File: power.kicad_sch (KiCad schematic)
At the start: 24 parts

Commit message: regulators
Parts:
- removed C_BECFC1, C_BECVTX1: 4u7, Capacitor_SMD:C_1206_3216Metric, symbol Device:C_Small
- removed C_BECFC2, C_BECVTX2: 100n, Capacitor_SMD:C_1206_3216Metric, symbol Device:C_Small
- removed C_BECFC3, C_BECVTX3: 1u, Capacitor_SMD:C_1206_3216Metric, symbol Device:C_Small
- removed C_BECFC4, C_BECFC5: 33u, Capacitor_SMD:C_1206_3216Metric, symbol Device:C_Small
- removed C_BECVTX4, C_BECVTX5, C_BECVTX6: 10u, Capacitor_SMD:C_1206_3216Metric, symbol Device:C_Small
- removed R_BECFC1: 41k2, Resistor_SMD:R_0402_1005Metric, symbol Device:R_Small
- removed R_BECFC2, R_BECVTX3: 10k, Resistor_SMD:R_0402_1005Metric, symbol Device:R_Small
- removed R_BECFC3: 12k1, Resistor_SMD:R_0402_1005Metric, symbol Device:R_Small
- removed R_BECVTX1: 10k5, Resistor_SMD:R_0402_1005Metric, symbol Device:R_Small
- removed R_BECVTX2: 80k6, Resistor_SMD:R_0402_1005Metric, symbol Device:R_Small
- removed U_BEC_FC_5V_1, U_BEC_VTX_9V_1: TPSM33625RDNR, RDN0011A-MFG, symbol custom_Library:TPSM33625RDNR
- added 5_C1, 5_C7: 10u, Capacitor_SMD:C_0603_1608Metric, symbol Device:C
- added 5_C10, 5_C11, 5_C4, 5_C5: 22u, Capacitor_SMD:C_0805_2012Metric, symbol Device:C
- added 5_C12, 5_C6: 75p, Capacitor_SMD:C_0402_1005Metric, symbol Device:C
- added 5_C2, 5_C3, 5_C8, 5_C9: 0.1u, Capacitor_SMD:C_0402_1005Metric, symbol Device:C
- added 5_R1, 5_R5: 511k, Resistor_SMD:R_0603_1608Metric, symbol Device:R
- added 5_R2, 5_R6: 105k, Resistor_SMD:R_0603_1608Metric, symbol Device:R
- added 5_R3, 5_R7: 100k, Resistor_SMD:R_0603_1608Metric, symbol Device:R
- added 5_R4: 13.3k, Resistor_SMD:R_0402_1005Metric, symbol Device:R
- added 5_R8: 7k, Resistor_SMD:R_0402_1005Metric, symbol Device:R
- added L1, L2: 10, Capacitor_SMD:C_0603_1608Metric, symbol Device:L
- added U4, U5: TPS54302DDCR, Package_TO_SOT_SMD:SOT-23-6, symbol Regulator_Switching:TPS54302
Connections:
- net 5V_BEC: now also 5_C10.1, 5_C11.1, 5_C12.1, 5_C4.1, 5_C5.1, 5_C6.1, 5_R3.1, 5_R7.1, L1.2, L2.2
- net GND: now also 5_C1.2, 5_C10.2, 5_C11.2, 5_C2.2, 5_C4.2, 5_C5.2, 5_C7.2, 5_C8.2, 5_R2.2, 5_R4.2, 5_R6.2, 5_R8.2, U4.1 (GND), U5.1 (GND)
- net Vin_LIPO: now also 5_C1.1, 5_C2.1, 5_C7.1, 5_C8.1, 5_R1.1, 5_R5.1, U4.3 (VIN), U5.3 (VIN)
- new net: 5_C3.2, L1.1, U4.2 (SW)
- new net: 5_C6.2, 5_R3.2, 5_R4.1, U4.4 (FB)
- new net: 5_R1.2, 5_R2.1, U4.5 (EN)
- new net: 5_C3.1, U4.6 (BOOT)
- new net: 5_C9.2, L2.1, U5.2 (SW)
- new net: 5_C12.2, 5_R7.2, 5_R8.1, U5.4 (FB)
- new net: 5_R5.2, 5_R6.1, U5.5 (EN)
- new net: 5_C9.1, U5.6 (BOOT)
- no-connect marks 5 -> 1
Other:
- note added: "BAT -> 5V"
- note added: "BAT -> 9V"
- note removed: "FC: BAT->5.1V@2.5A: TPSM33625RDNR"
- note removed: "VTX: BAT->9V@2.5A (DJI:~1A@9V) TPSM33625RDNR"

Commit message: boom boom
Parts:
- L1: value 10 -> 10u
- L2: value 10 -> 15u
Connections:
- net 5V_BEC: no longer 5_C10.1, 5_C11.1, 5_C12.1, 5_R7.1, L2.2
- new net 9V_BEC: 5_C10.1, 5_C11.1, 5_C12.1, 5_R7.1, L2.2
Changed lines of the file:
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@@
 		)
 	)
-	(global_label "5V_BEC"
+	(global_label "9V_BEC"
 		(shape input)
 		(at 260.35 119.38 0)
@@
 			)
 		)
-		(property "Value" "10"
+		(property "Value" "10u"
 			(at 226.06 41.91 90)
 			(effects
@@
 			)
 		)
-		(property "Value" "10"
+		(property "Value" "15u"
 			(at 226.06 116.84 90)
 			(effects

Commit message: labels
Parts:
- 5V_C2: renamed from 5_C2; value 0.1u -> 0u1
- 5V_C3: renamed from 5_C3; value 0.1u -> 0u1
- 9V_C2: renamed from 5_C8; value 0.1u -> 0u1
- 9V_C3: renamed from 5_C9; value 0.1u -> 0u1
- renumbered C2_LDO1 to 3V3_C2, C1_LDO1 to 3v3_C1, 5_C1 to 5V_C1, 5_C4 to 5V_C4, 5_C5 to 5V_C5, 5_C6 to 5V_C6, L1 to 5V_L1, 5_R1 to 5V_R1, 5_R2 to 5V_R2, 5_R3 to 5V_R3, 5_R4 to 5V_R4, 5_C7 to 9V_C1, 5_C10 to 9V_C4, 5_C11 to 9V_C5, 5_C12 to 9V_C6, L2 to 9V_L1, 5_R5 to 9V_R1, 5_R6 to 9V_R2, 5_R7 to 9V_R3, 5_R8 to 9V_R4, U_LDO1 to U_3V3
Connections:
- net 3V3_MCU_OSD renamed 3.3V
- net Vin_LIPO renamed LIPO
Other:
- note added: "5V -> 3V3 @500mA"
- note removed: "FC LDO: 5V bus -> 3V3 @500mA"

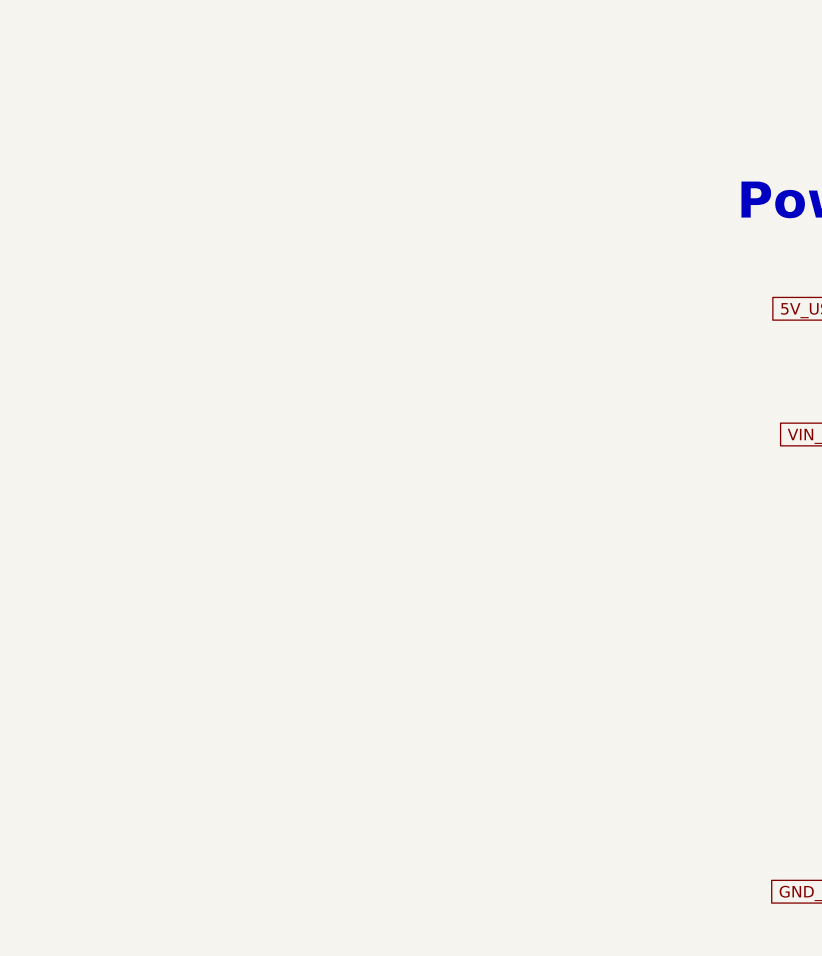
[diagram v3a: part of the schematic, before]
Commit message: power mux
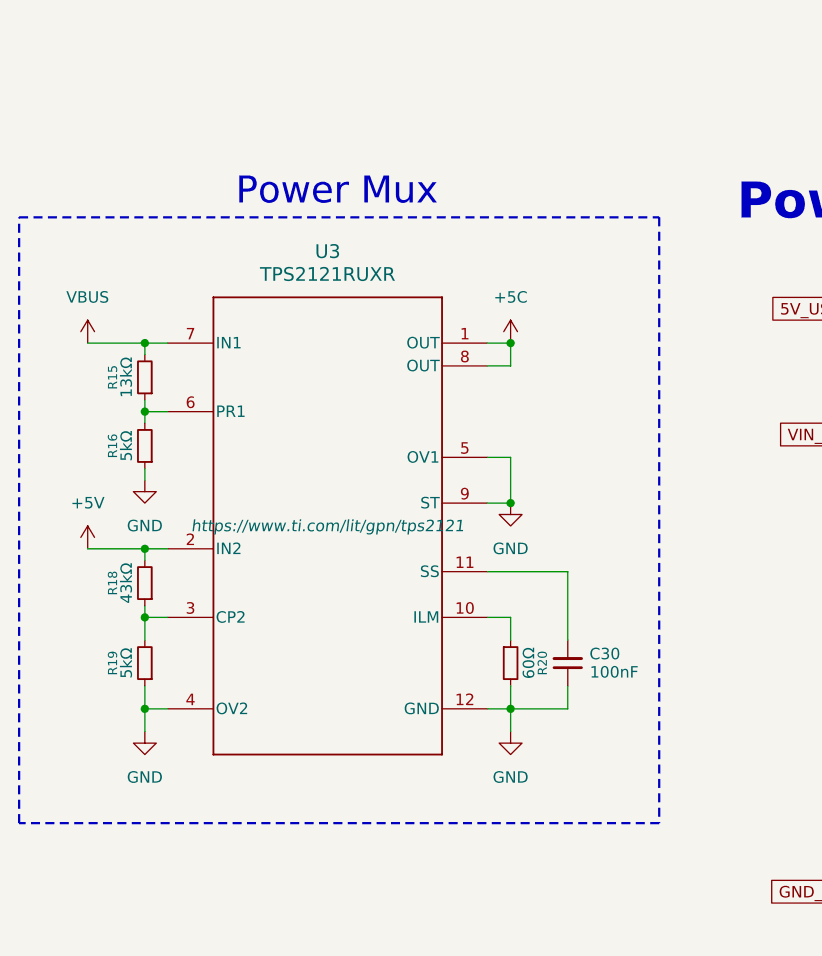
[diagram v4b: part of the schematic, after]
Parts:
- added C30: 100nF, Capacitor_SMD:C_0603_1608Metric, symbol Device:C_Small
- added R15: 13kΩ, Resistor_SMD:R_0603_1608Metric, symbol Device:R_Small
- added R16, R19: 5kΩ, Resistor_SMD:R_0603_1608Metric, symbol Device:R_Small
- added R18: 43kΩ, Resistor_SMD:R_0603_1608Metric, symbol Device:R_Small
- added R20: 60Ω, Resistor_SMD:R_0603_1608Metric, symbol Device:R_Small
- added U3: TPS2121RUXR, TPS2121RUXR:RUX0012A, symbol ul_TPS2121RUXR:TPS2121RUXR
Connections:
- net GND: now also C30.1, R16.1, R19.1, R20.2, U3.12 (GND), U3.4 (OV2), U3.5 (OV1), U3.9 (ST)
- new net: R15.1, R16.2, U3.6 (PR1)
- new net: R20.1, U3.10 (ILM)
- new net: C30.2, U3.11 (SS)
- new net: R18.1, R19.2, U3.3 (CP2)
- new net +5C: U3.1 (OUT), U3.8 (OUT)
- new net +5V: R18.2, U3.2 (IN2)
- new net VBUS: R15.2, U3.7 (IN1)
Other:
- note added: "Power Mux"

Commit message: single sheet
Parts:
- removed 3V3_C2, 3v3_C1: 4u7, Capacitor_SMD:C_0805_2012Metric, symbol Device:C_Small
- removed 5V_C1, 9V_C1: 10u, Capacitor_SMD:C_0603_1608Metric, symbol Device:C
- removed 5V_C2, 5V_C3, 9V_C2, 9V_C3: 0u1, Capacitor_SMD:C_0402_1005Metric, symbol Device:C
- removed 5V_C4, 5V_C5, 9V_C4, 9V_C5: 22u, Capacitor_SMD:C_0805_2012Metric, symbol Device:C
- removed 5V_C6, 9V_C6: 75p, Capacitor_SMD:C_0402_1005Metric, symbol Device:C
- removed 5V_L1: 10u, Capacitor_SMD:C_0603_1608Metric, symbol Device:L
- removed 5V_R1, 9V_R1: 511k, Resistor_SMD:R_0603_1608Metric, symbol Device:R
- removed 5V_R2, 9V_R2: 105k, Resistor_SMD:R_0603_1608Metric, symbol Device:R
- removed 5V_R3, 9V_R3: 100k, Resistor_SMD:R_0603_1608Metric, symbol Device:R
- removed 5V_R4: 13.3k, Resistor_SMD:R_0402_1005Metric, symbol Device:R
- removed 9V_L1: 15u, Capacitor_SMD:C_0603_1608Metric, symbol Device:L
- removed 9V_R4: 7k, Resistor_SMD:R_0402_1005Metric, symbol Device:R
- removed C30: 100nF, Capacitor_SMD:C_0603_1608Metric, symbol Device:C_Small
- removed D_5V, D_5V_USB: B340A-13-F, custom_Library:Schottky BA340 SMA_L4.4-W2.6-LS5.0-RD, symbol custom_Library:B340A-13-F
- removed R15: 13kΩ, Resistor_SMD:R_0603_1608Metric, symbol Device:R_Small
- removed R16, R19: 5kΩ, Resistor_SMD:R_0603_1608Metric, symbol Device:R_Small
- removed R18: 43kΩ, Resistor_SMD:R_0603_1608Metric, symbol Device:R_Small
- removed R20: 60Ω, Resistor_SMD:R_0603_1608Metric, symbol Device:R_Small
- removed U3: TPS2121RUXR, TPS2121RUXR:RUX0012A, symbol ul_TPS2121RUXR:TPS2121RUXR
- removed U4, U5: TPS54302DDCR, Package_TO_SOT_SMD:SOT-23-6, symbol Regulator_Switching:TPS54302
- removed U_3V3: LP5912-3.3DRVR, custom_Library:LP59123.3_SON65P200X200X80-7N, symbol custom_Library:LP5912-3.3DRVR
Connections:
- no-connect marks 1 -> 0
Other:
- note removed: "5V -> 3V3 @500mA"
- note removed: "BAT -> 5V"
- note removed: "BAT -> 9V"
- note removed: "Diodes: 40V/3A 500mV 850mW"
- note removed: "Power Mux"
- note removed: "Power Path"
